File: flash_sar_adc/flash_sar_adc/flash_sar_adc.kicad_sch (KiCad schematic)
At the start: 62 parts, among them J1 Conn_02x06_Matched, J2 Conn_02x06_Matched, U1 LM339LVDR, U10 RH-5000, U2 LM339LVDR, U3 OPA843xDBV, U5 HL-BNC-KHDA, U6 RH-5000, U7 HL-BNC-KHDA, U8 RH-5000, U9 RH-5000

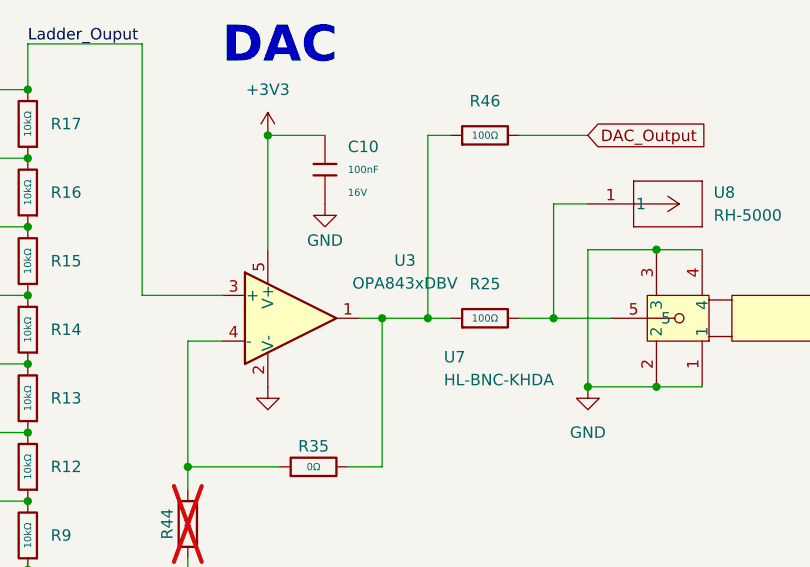
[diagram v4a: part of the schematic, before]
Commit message: fixed a few more silkscreen errors
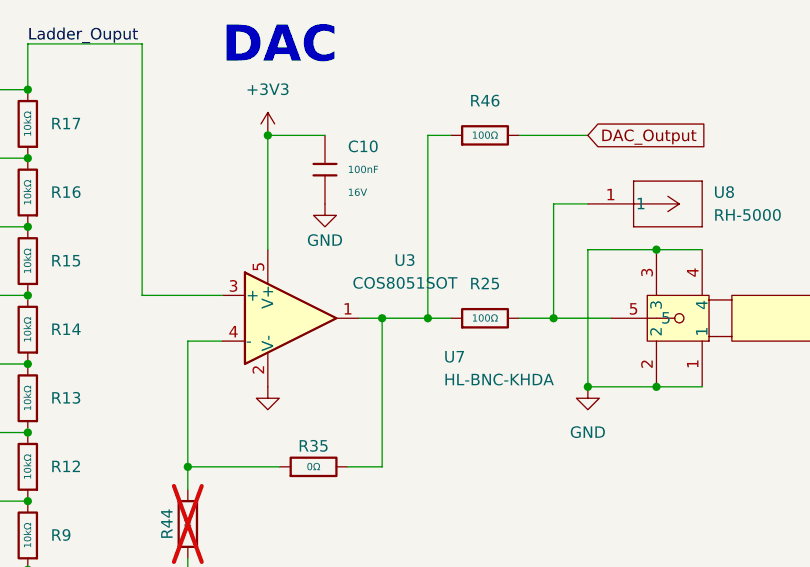
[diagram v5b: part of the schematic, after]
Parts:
- U3: value OPA843xDBV -> COS8051SOT
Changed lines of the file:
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@@
 		(polyline
 			(pts
-				(xy 13.97 119.38) (xy 204.47 119.38) (xy 204.47 165.1) (xy 167.64 165.1) (xy 167.64 196.85) (xy 13.97 196.85)
+				(xy 146.05 16.51) (xy 177.8 16.51) (xy 177.8 97.79) (xy 146.05 97.79)
 			)
 			(stroke
@@
 		(polyline
 			(pts
-				(xy 180.34 22.86) (xy 200.66 22.86) (xy 200.66 95.25) (xy 180.34 95.25)
+				(xy 13.97 119.38) (xy 204.47 119.38) (xy 204.47 165.1) (xy 167.64 165.1) (xy 167.64 196.85) (xy 13.97 196.85)
 			)
 			(stroke
@@
 		(polyline
 			(pts
-				(xy 146.05 16.51) (xy 177.8 16.51) (xy 177.8 97.79) (xy 146.05 97.79)
+				(xy 180.34 22.86) (xy 200.66 22.86) (xy 200.66 95.25) (xy 180.34 95.25)
 			)
 			(stroke
@@
 			)
 		)
-		(property "Value" "OPA843xDBV"
+		(property "Value" "COS8051SOT"
 			(at 157.48 151.0598 0)
 			(effects
